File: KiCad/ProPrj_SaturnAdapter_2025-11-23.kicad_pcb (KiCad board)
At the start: 2 copper layers, 51.5 x 41.8 mm, 32 parts

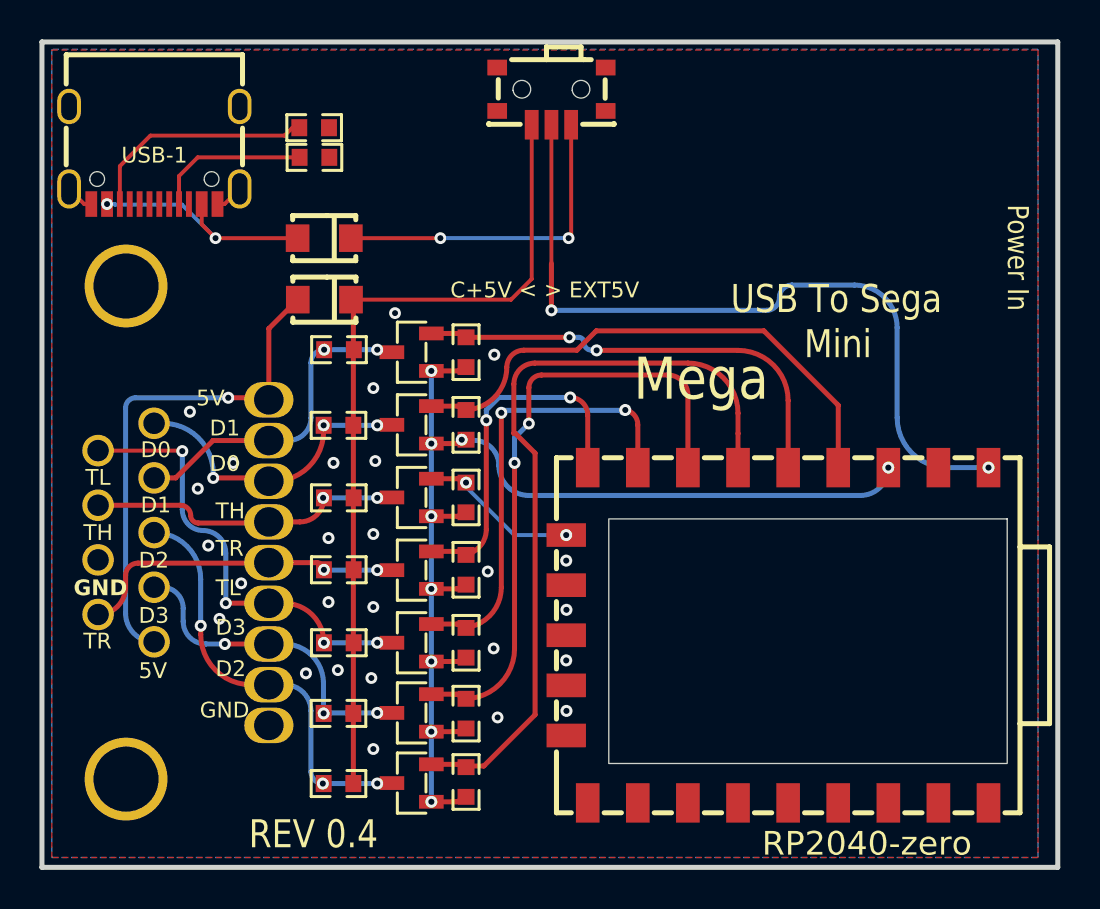
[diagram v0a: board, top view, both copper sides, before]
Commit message: REV0.5 - Move USB and Switch around, shrink board size to more closely match REV0.4
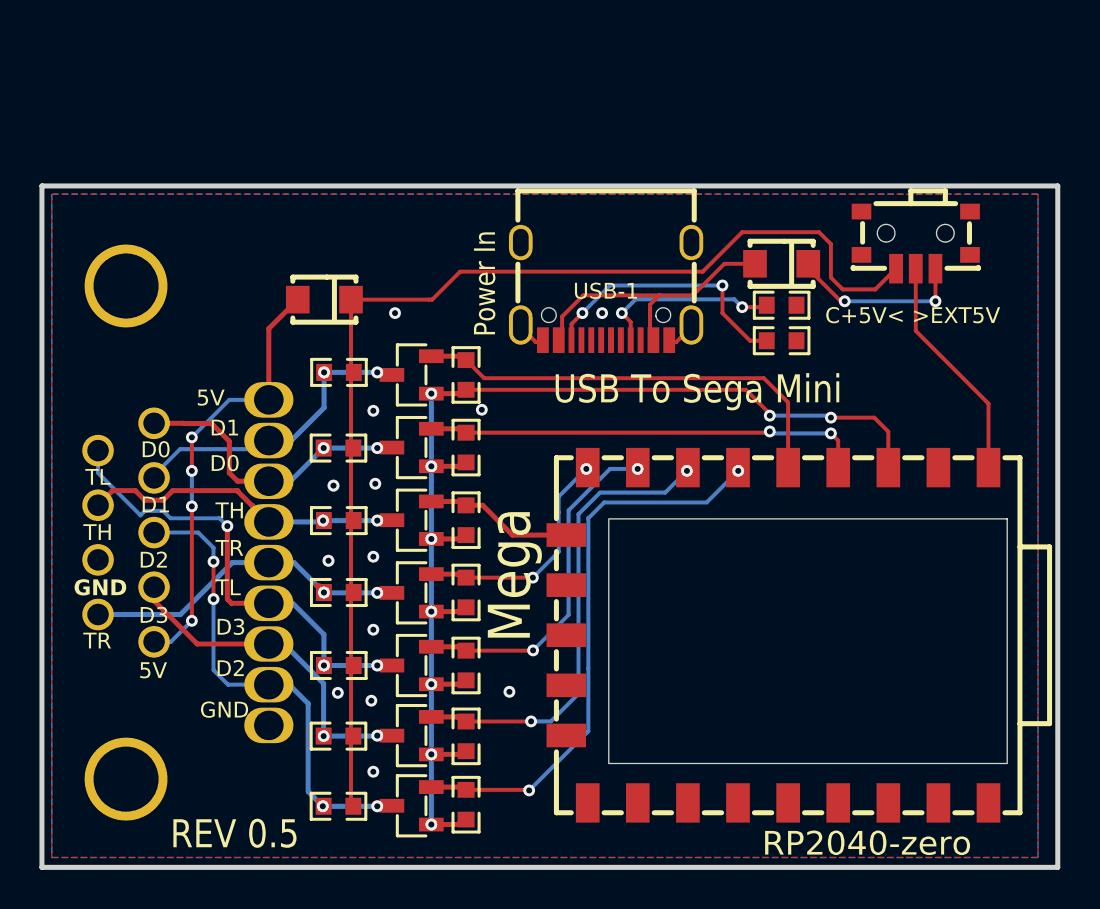
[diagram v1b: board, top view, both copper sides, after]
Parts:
- moved R15 26.0 mm to (160.0, 97.8)
- moved R16 24.8 mm to (160.0, 96.0)
- moved USB-1 23.9 mm to (151.1, 95.3)
- moved C2 23.2 mm to (160.0, 93.9)
- moved SW1 19.9 mm to (166.8, 92.7)
- moved G*** 10.9 mm to (166.6, 97.5)
- moved Q1 1.15 mm to (141.2, 99.5)
- moved Q2 1.15 mm to (141.2, 103.2)
- moved Q3 1.15 mm to (141.2, 106.9)
- moved Q4 1.15 mm to (141.2, 110.6)
- moved Q5 1.15 mm to (141.2, 121.4)
- moved Q6 1.15 mm to (141.2, 117.8)
- moved Q7 1.15 mm to (141.2, 114.3)
- moved R1 1.15 mm to (144.0, 99.5)
- moved R10 1.15 mm to (144.0, 121.3)
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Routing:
- net PICO+5V: track 39.3 -> 12.2 mm, vias 2 -> 0
- net C+5V: track 42.5 -> 57.5 mm
- net LO_D2: track 39.9 -> 28.6 mm, vias 0 -> 2
- net LO_D3: track 32.0 -> 23.7 mm
- net EXT5V: track 16.8 -> 9.88 mm
- net LO_TR: track 18.2 -> 11.6 mm
- net LO_TL: track 23.4 -> 17.3 mm
- net LO_D0: track 27.5 -> 22.2 mm, vias 0 -> 2
- net IN+5V: track 25.9 -> 22.2 mm, vias 1 -> 4
- net D2: track 21.6 -> 25.2 mm, vias 3 -> 4
- net OUT+5V: track 12.4 -> 15.0 mm, vias 2 -> 0
- net D3: track 16.5 -> 18.3 mm, vias 3 -> 2
- net CC2: track 11.8 -> 13.6 mm, vias 0 -> 2
- net CC1: track 7.92 -> 9.50 mm, vias 0 -> 2
- net TL: track 22.6 -> 24.2 mm, vias 4 -> 3
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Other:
- board size 51.5 x 41.8 mm -> 51.5 x 34.5 mm
- board text added: "C+5V< >EXT5V"
- board text added: "REV 0.5"
- board text removed: "C+5V < > EXT5V"
- board text removed: "REV 0.4"

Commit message: REV0.5 - Moved two of the SOT-23-3Ps to make room for a further shifting of the USB C port towards the controller plug
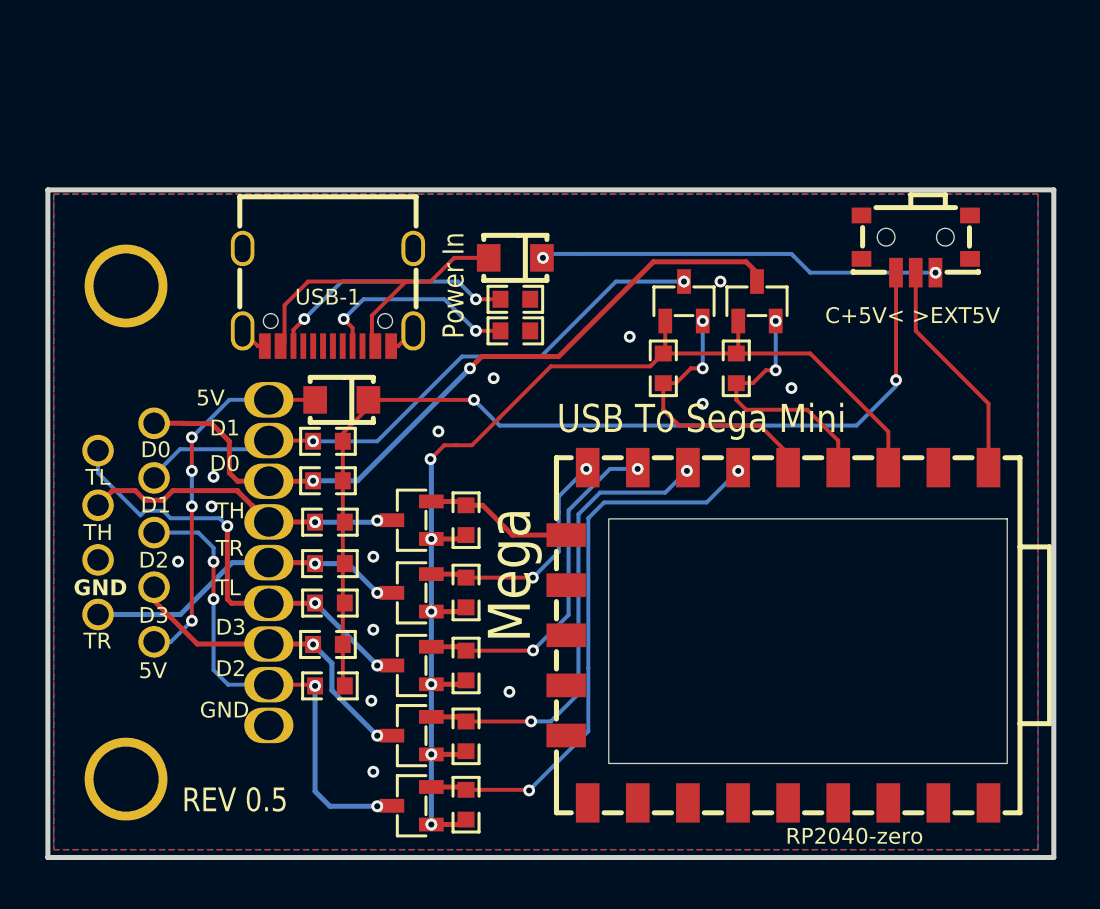
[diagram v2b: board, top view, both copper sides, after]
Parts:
- moved Q2 19.0 mm to (158.8, 95.8), turned to -90 degrees
- moved Q1 14.3 mm to (155.1, 95.8), turned to -90 degrees
- moved R3 14.3 mm to (157.7, 99.2), turned to -90 degrees
- moved USB-1 14.1 mm to (137.0, 95.6)
- moved R15 13.7 mm to (146.5, 95.7)
- moved R16 13.6 mm to (146.5, 97.3)
- moved C2 13.5 mm to (146.5, 93.6)
- moved R1 10.0 mm to (154.0, 99.2), turned to -90 degrees
- moved R9 6.12 mm to (137.1, 115.3)
- moved C1 5.16 mm to (137.7, 100.8)
- moved R11 4.68 mm to (137.0, 113.2)
- moved R2 3.54 mm to (137.0, 102.9)
- moved R13 3.20 mm to (137.1, 111.1)
- moved REF** 1.81 mm to (136.9, 93.6)
- moved R4 1.74 mm to (137.0, 104.9)
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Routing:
- net D0: track 16.2 -> 39.8 mm
- net D1: track 15.5 -> 32.1 mm
- net EXT5V: track 9.88 -> 20.4 mm
- net LO_D0: track 22.2 -> 13.0 mm
- net C+5V: track 57.5 -> 48.7 mm, vias 0 -> 2
- net LO_D1: track 22.2 -> 14.0 mm, vias 0 -> 2
- net IN+5V: track 22.2 -> 19.3 mm
- net OUT+5V: track 15.0 -> 17.6 mm
- net D2: track 25.2 -> 27.1 mm
- net TL: track 24.2 -> 22.5 mm
- net VCC: track 57.4 -> 58.8 mm, vias 9 -> 6
- net CC1: track 9.50 -> 10.6 mm
- net CC2: track 13.6 -> 12.7 mm
- net PICO+5V: track 12.2 -> 11.4 mm
- net TR: track 17.2 -> 16.7 mm
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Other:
- board size 51.5 x 34.5 mm -> 51 x 33.8 mm

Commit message: Further adjustment of USB port placement and trace optimisation (All curved traces replaced with 45 degrees)
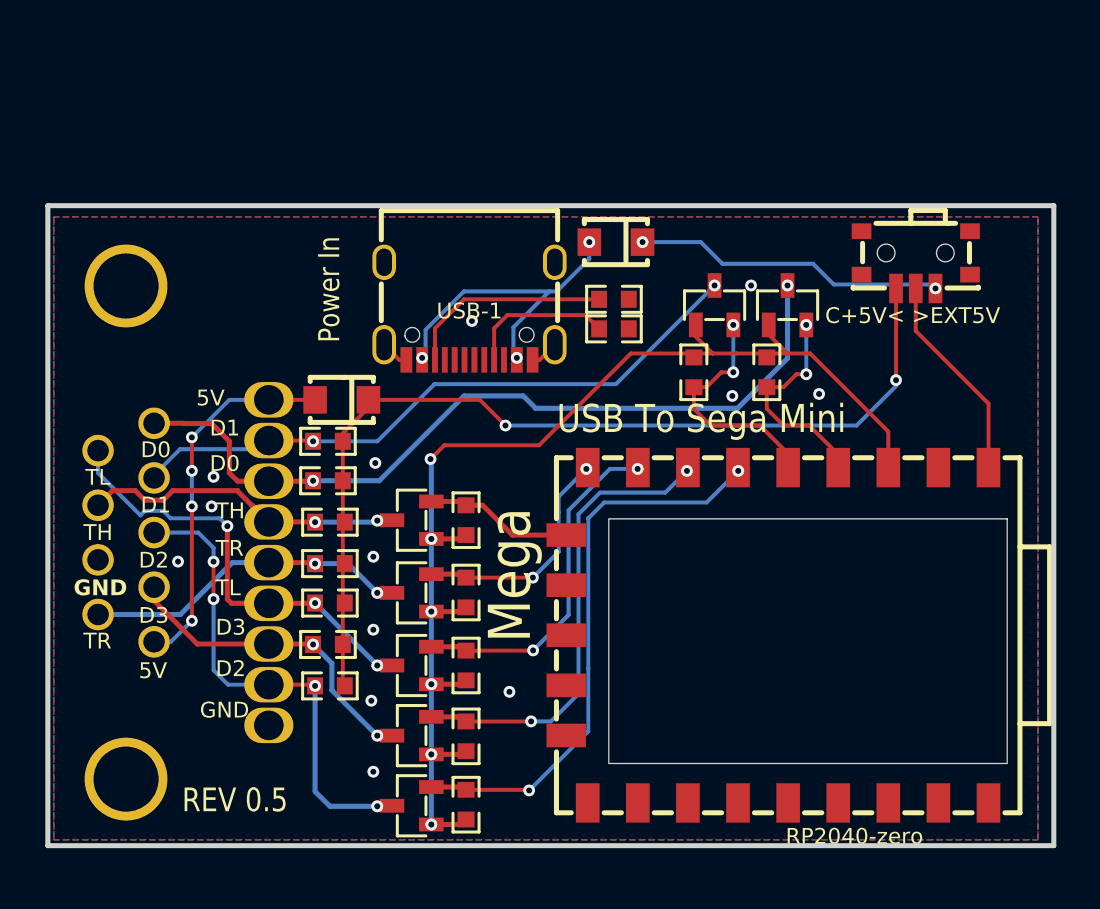
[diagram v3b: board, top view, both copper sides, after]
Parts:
- moved REF** 7.41 mm to (144.3, 93.9)
- moved USB-1 7.21 mm to (144.2, 96.3)
- moved C2 5.16 mm to (151.6, 92.8)
- moved R16 5.00 mm to (151.5, 97.2)
- moved R15 5.00 mm to (151.5, 95.7)
- moved Q2 1.56 mm to (160.3, 96.0)
- moved R1 1.56 mm to (155.6, 99.4)
- moved R3 1.56 mm to (159.2, 99.4)
- moved Q1 1.56 mm to (156.6, 96.0)
- moved SW1 0.80 mm to (166.8, 93.7)
- moved G*** 0.32 mm to (166.7, 97.8)
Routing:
- net EXT5V: track 20.4 -> 15.8 mm
- net CC1: track 10.6 -> 7.38 mm, vias 2 -> 0
- net D0: track 39.8 -> 42.9 mm
- net CC2: track 12.7 -> 10.4 mm, vias 2 -> 0
- net LO_D0: track 13.0 -> 11.1 mm
- net LO_D1: track 14.0 -> 12.2 mm
- net D1: track 32.1 -> 33.7 mm
- net OUT+5V: track 17.6 -> 16.3 mm, vias 0 -> 3
- net PICO+5V: track 11.4 -> 10.6 mm
- net C+5V: track 48.7 -> 47.9 mm
- net VCC: track 58.8 -> 59.4 mm
- net GND: vias 14 -> 13
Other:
- board size 51 x 33.8 mm -> 51 x 32.4 mm

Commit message: Add mounting holes for eventual 3d printed case
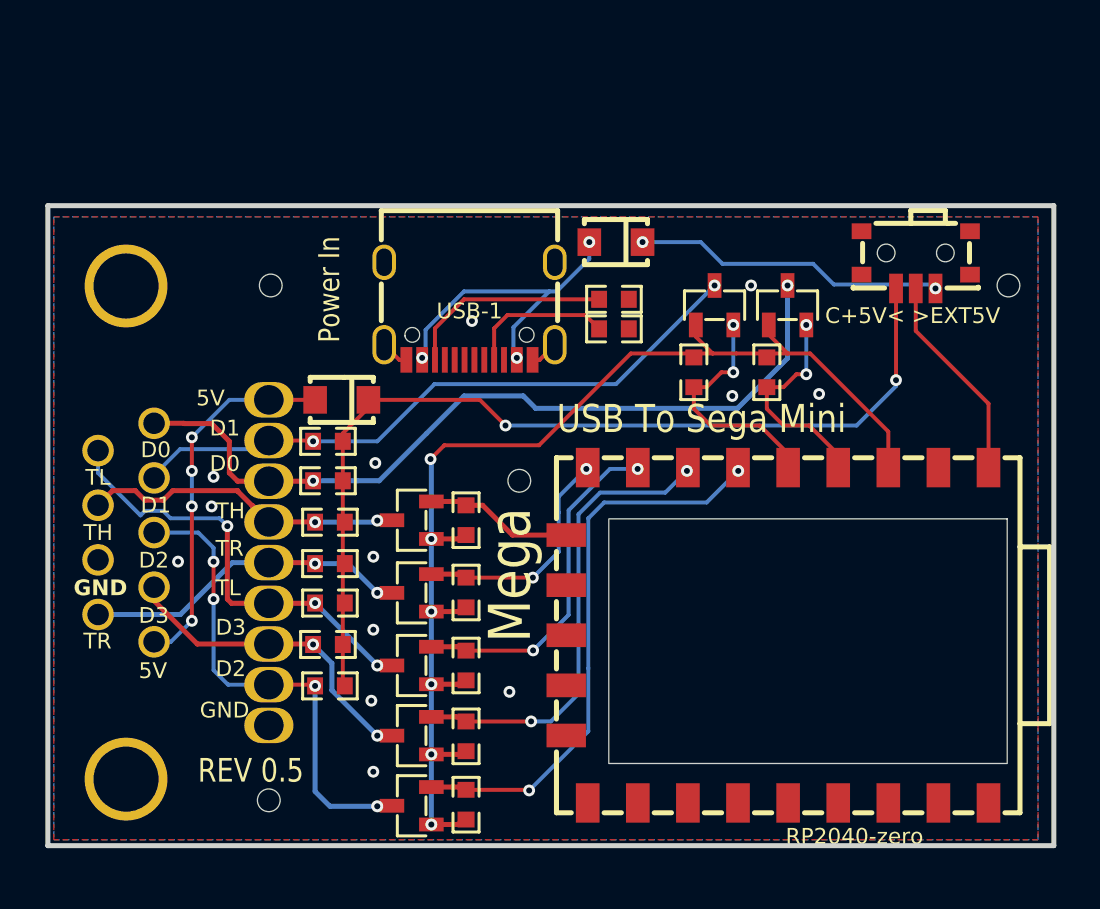
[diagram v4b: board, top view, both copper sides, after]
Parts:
- added ?: , , F.Cu at (171.5, 95.0)
- added REF**: ToolingHole_1.152mm, MountingHole:ToolingHole_1.152mm, F.Cu at (134.1, 95.0)
- added REF**: ToolingHole_1.152mm, MountingHole:ToolingHole_1.152mm, F.Cu at (134.0, 121.1)
- added REF**: ToolingHole_1.152mm, MountingHole:ToolingHole_1.152mm, F.Cu at (146.7, 104.9)

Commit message: Add Change to central mounting hole for future case
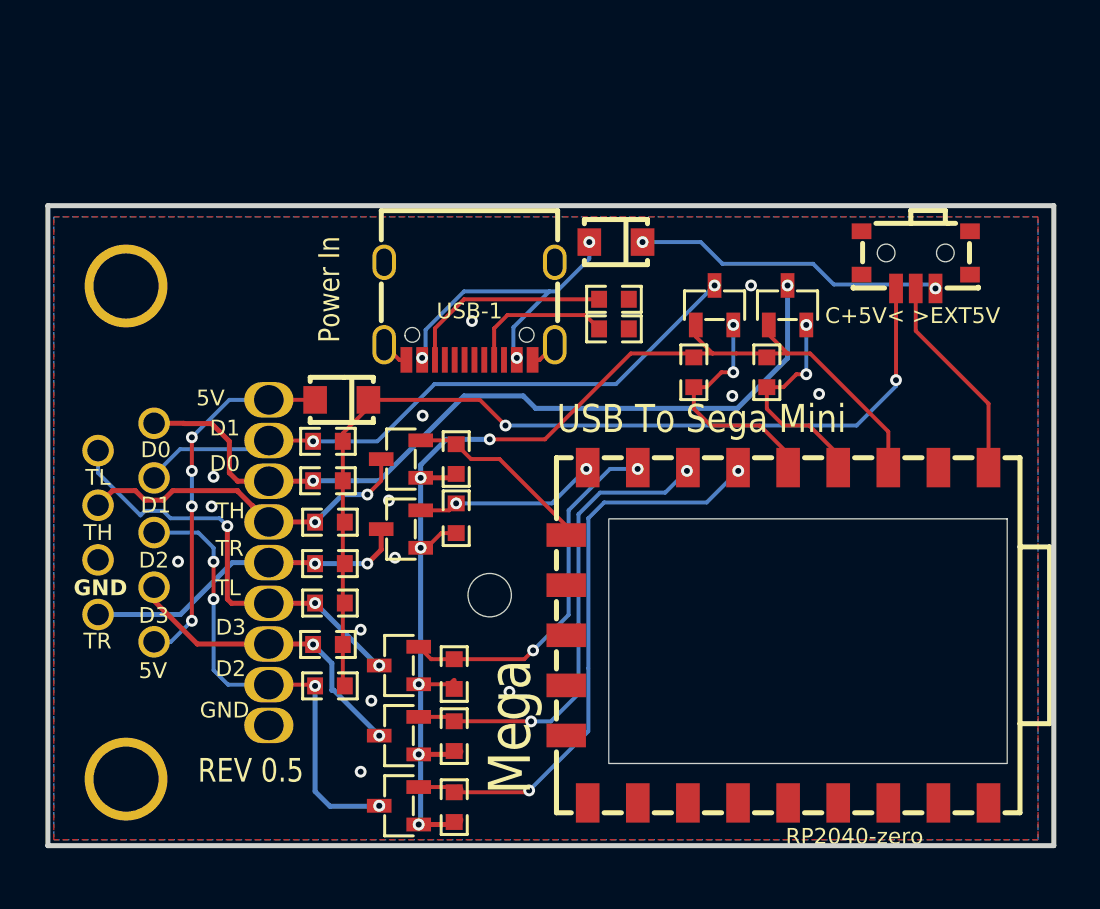
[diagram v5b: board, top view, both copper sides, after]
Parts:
- removed ?: , 
- removed the REF** at (134.1, 95.0)
- removed the REF** at (134.0, 121.1)
- removed the REF** at (146.7, 104.9)
- added REF**: MountingHole_2.2mm_M2_DIN965, MountingHole:MountingHole_2.2mm_M2_DIN965, F.Cu at (145.2, 110.7)
- moved R7 3.80 mm to (143.5, 106.8)
- moved Q4 3.28 mm to (140.7, 107.3)
- moved Q3 3.15 mm to (140.7, 103.8)
- moved R5 3.14 mm to (143.5, 103.8)
- moved R14 0.74 mm to (143.4, 114.7)
- moved Q5 0.64 mm to (140.6, 121.4)
- moved Q6 0.64 mm to (140.6, 117.8)
- moved Q7 0.64 mm to (140.6, 114.3)
- moved R10 0.61 mm to (143.4, 121.4)
- moved R12 0.60 mm to (143.4, 117.8)
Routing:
- net VCC: track 59.4 -> 62.2 mm
- net LO_TR: track 11.6 -> 9.27 mm
- net LO_TH: track 7.63 -> 9.37 mm
- net TH: track 16.4 -> 17.8 mm
- net LO_TL: track 17.3 -> 18.5 mm
- net LO_D2: track 28.6 -> 29.6 mm
- net D2: track 27.1 -> 26.3 mm
- net D3: track 18.4 -> 17.7 mm
- net TL: track 22.5 -> 21.8 mm
- net LO_D3: track 23.7 -> 24.3 mm
- net GND: vias 13 -> 14

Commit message: Updated schematic for neatness, and further shrank the PCB with the USB-C port brought closer to center
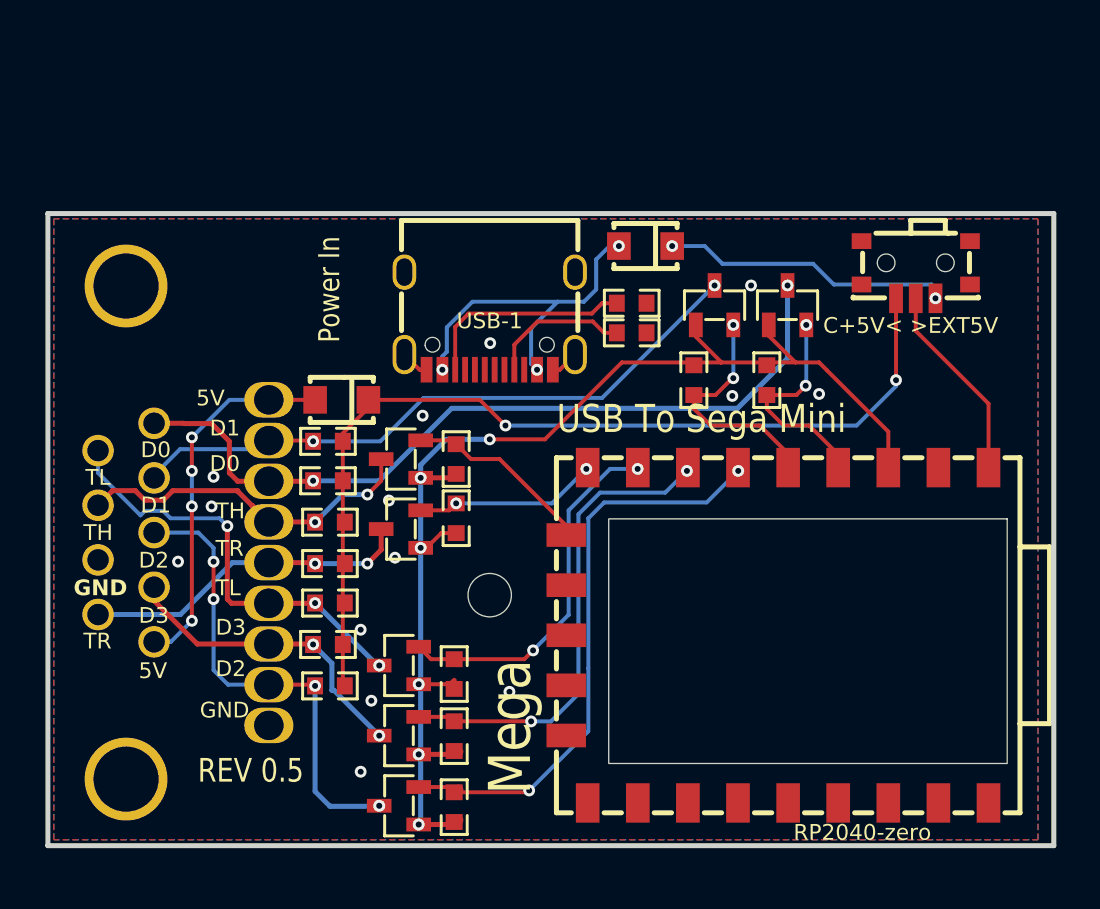
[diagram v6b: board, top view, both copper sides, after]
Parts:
- moved C2 1.51 mm to (153.1, 93.0)
- moved REF** 1.22 mm to (145.3, 94.6)
- moved USB-1 1.14 mm to (145.2, 96.8)
- moved R15 0.92 mm to (152.4, 95.9)
- moved R16 0.92 mm to (152.4, 97.4)
- moved G*** 0.78 mm to (167.2, 98.4)
- moved SW1 0.50 mm to (166.8, 94.2)
- moved R1 0.40 mm to (155.6, 99.8)
- moved R3 0.40 mm to (159.2, 99.8)
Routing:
- net OUT+5V: track 16.3 -> 17.7 mm
- net EXT5V: track 15.8 -> 14.7 mm
- net VCC: track 62.2 -> 63.0 mm
- net D0: track 42.9 -> 42.4 mm
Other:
- board size 51 x 32.4 mm -> 51 x 32 mm

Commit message: Fix capacitors (Had it in line with the 5v rail rather than properly smoothing [facepalm ]
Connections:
- C1 pad 2: IN+5V -> GND
- C2 pad 2: OUT+5V -> GND
- CN1 pad 5: IN+5V -> C+5V
- U2 pad 1: IN+5V -> C+5V
- USB-1 pad A4B9: OUT+5V -> EXT5V
- USB-1 pad B4A9: OUT+5V -> EXT5V
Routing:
- net C+5V: track 47.9 -> 69.5 mm, vias 2 -> 7
- net EXT5V: track 14.7 -> 35.1 mm, vias 2 -> 5
- net IN+5V: track 19.3 -> 0.00 mm, vias 4 -> 0
- net OUT+5V: track 17.7 -> 0.00 mm, vias 3 -> 0
